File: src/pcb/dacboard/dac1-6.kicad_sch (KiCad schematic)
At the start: 18 parts, among them U10 AD5791BRUZ, U11 AD8676xR, U12 AD8676xR, U13 AD5791BRUZ, U14 AD8676xR, U15 AD5791BRUZ, U16 AD8676xR, U17 AD5791BRUZ, U18 AD8676xR, U19 AD5791BRUZ, U20 AD8676xR, U21 AD5791BRUZ

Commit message: dacboard routing
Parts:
- C22, C23, C24, C25, C26, C27: footprint (none) -> Capacitor_SMD:C_0603_1608Metric_Pad1.08x0.95mm_HandSolder
- U10, U13, U15, U17, U19, U21: footprint RU_20_ADI -> Package_SO:TSSOP-20_4.4x6.5mm_P0.65mm

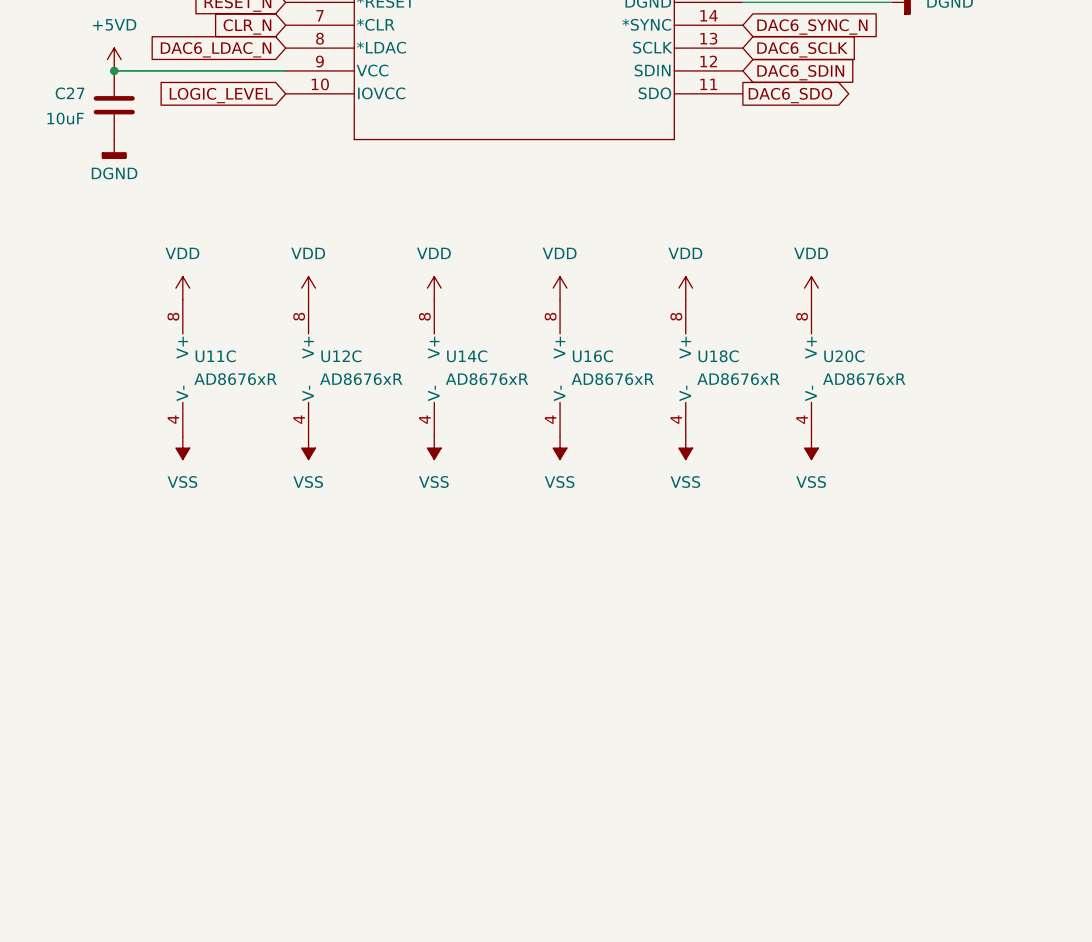
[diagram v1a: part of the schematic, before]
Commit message: adding more capacitors to analog side
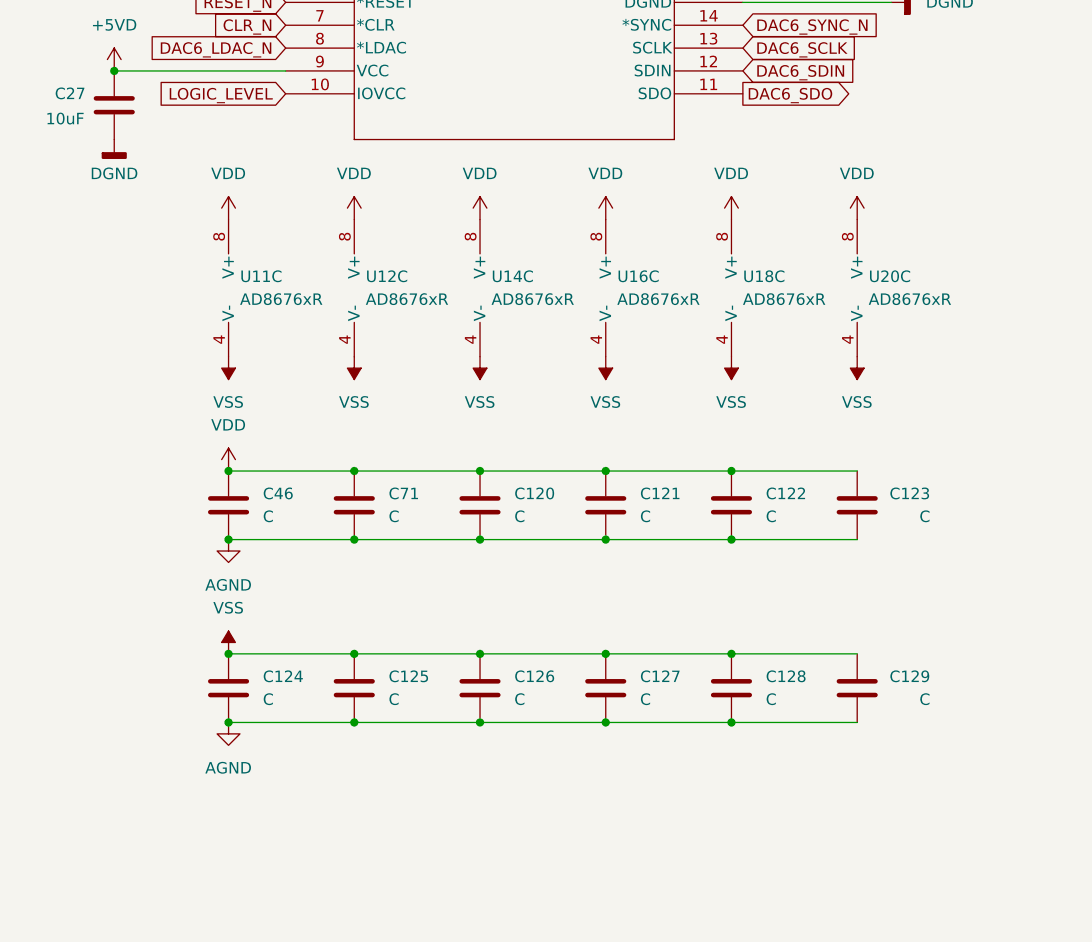
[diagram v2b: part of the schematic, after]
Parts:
- added C120, C121, C122, C123, C124, C125, C126, C127, C128, C129, C46, C71: C, Capacitor_SMD:C_0402_1005Metric_Pad0.74x0.62mm_HandSolder, symbol Device:C
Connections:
- net AGND: now also C120.2, C121.2, C122.2, C123.2, C124.2, C125.2, C126.2, C127.2, C128.2, C129.2, C46.2, C71.2
- net VDD: now also C120.1, C121.1, C122.1, C123.1, C46.1, C71.1
- net VSS: now also C124.1, C125.1, C126.1, C127.1, C128.1, C129.1
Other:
- moved on the sheet: U11C, U12C, U14C, U16C, U18C, U20C

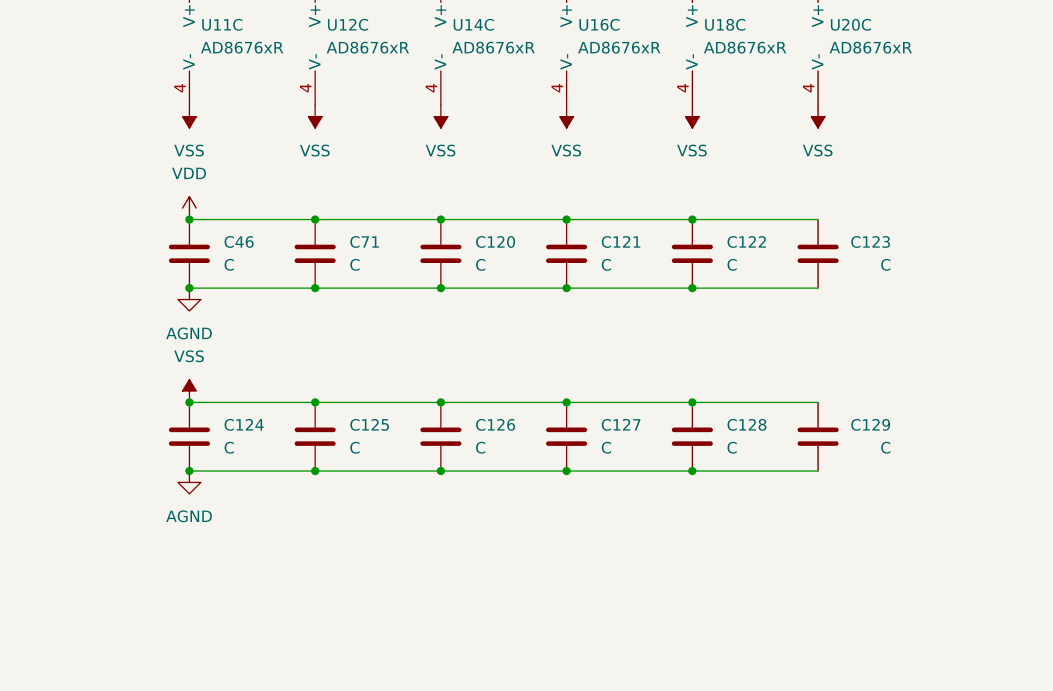
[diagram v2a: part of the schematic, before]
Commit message: more capacitors
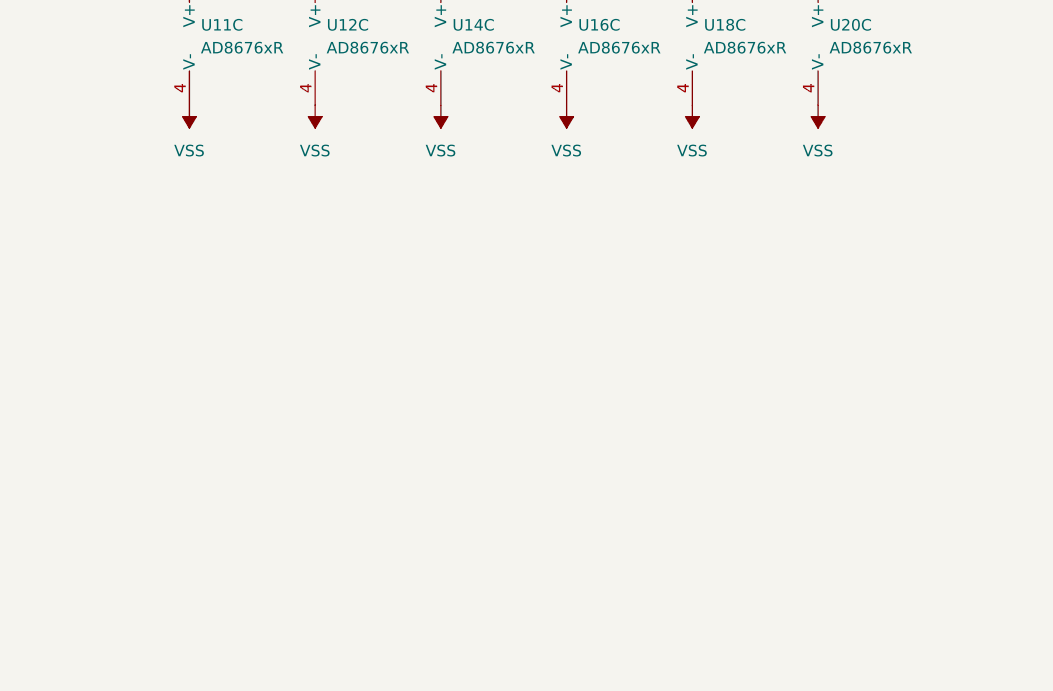
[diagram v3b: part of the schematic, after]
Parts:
- removed C120, C121, C122, C123, C124, C125, C126, C127, C128, C129, C46, C71: C, Capacitor_SMD:C_0402_1005Metric_Pad0.74x0.62mm_HandSolder, symbol Device:C

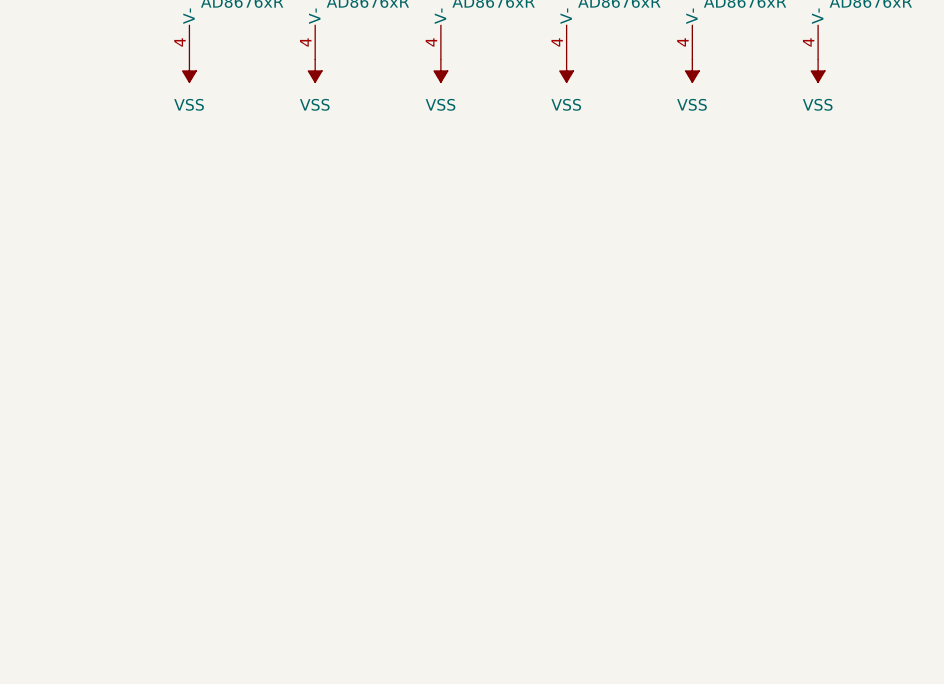
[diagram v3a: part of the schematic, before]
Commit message: got rid of all drc errors
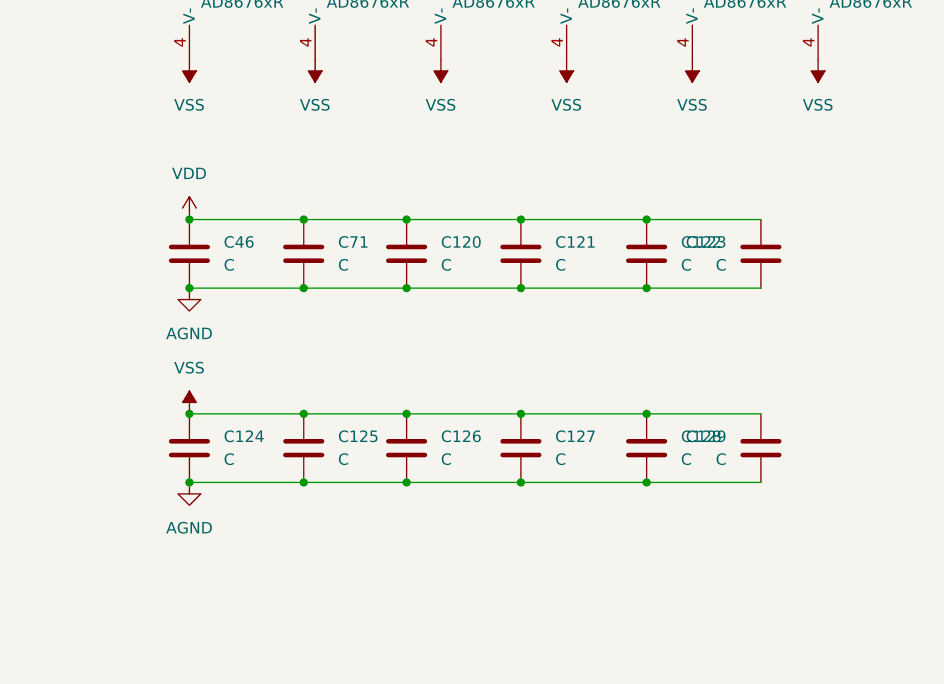
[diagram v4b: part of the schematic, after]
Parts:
- added C120, C121, C122, C123, C124, C125, C126, C127, C128, C129, C46, C71: C, Capacitor_SMD:C_0402_1005Metric_Pad0.74x0.62mm_HandSolder, symbol Device:C
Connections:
- net AGND: now also C120.2, C121.2, C122.2, C123.2, C124.2, C125.2, C126.2, C127.2, C128.2, C129.2, C46.2, C71.2
- net VDD: now also C120.1, C121.1, C122.1, C123.1, C46.1, C71.1
- net VSS: now also C124.1, C125.1, C126.1, C127.1, C128.1, C129.1
